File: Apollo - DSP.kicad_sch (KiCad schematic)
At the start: 27 parts, among them J1 USB_C_Receptacle_USB2.0, U1 NCP115ASN330T2G, U2 USBLC6-2SC6, U3 NCP115ASN330T2G

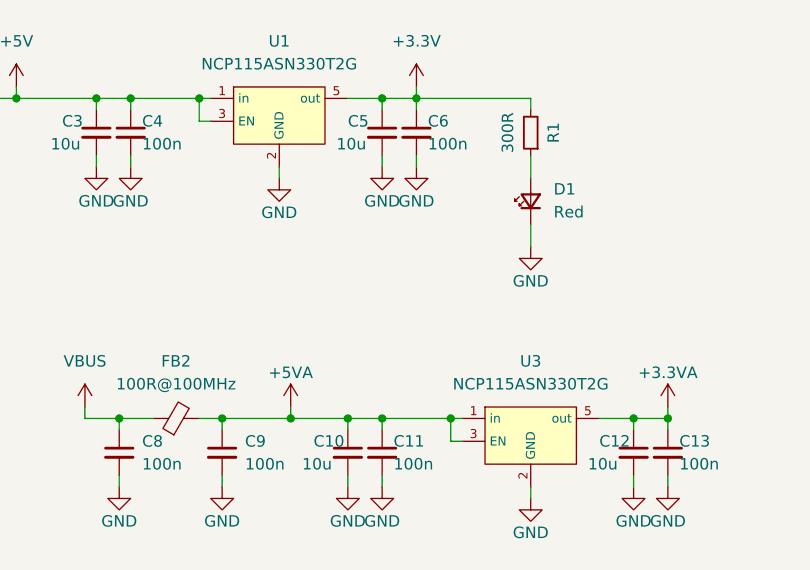
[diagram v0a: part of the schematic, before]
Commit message: made analog circuitry a bit more compact moved whole board
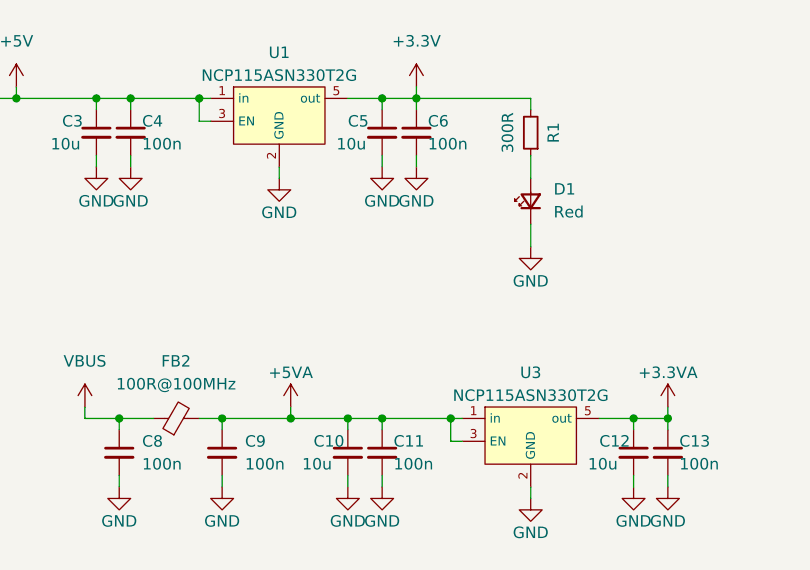
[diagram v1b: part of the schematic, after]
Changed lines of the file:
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@@
-    )
-  )
-  (symbol (lib_id "NCP115ASN330T2G:NCP115ASN330T2G") (at 160.02 71.12 0) (unit 1)
-    (in_bom yes) (on_board yes) (dnp no) (fields_autoplaced)
-    (property "Reference" "U1" (at 160.02 63.5 0)
-      (effects (font (size 1.27 1.27)))
-    )
-    (property "Value" "NCP115ASN330T2G" (at 160.02 66.04 0)
-      (effects (font (size 1.27 1.27)))
-    )
-    (property "Footprint" "NCP115ASN330T2G:NCP115ASN330T2G" (at 161.29 62.23 0)
-      (effects (font (size 1.27 1.27)) hide)
-    )
-    (property "Datasheet" "https://www.onsemi.com/pdf/datasheet/ncp115-d.pdf" (at 160.02 59.69 0)
-      (effects (font (size 1.27 1.27)) hide)
-    )
-    (pin "1")
-    (pin "2")
-    (pin "3")
-    (pin "5")
-    (instances
-      (project "Apollo - DSP"
-        (path "/e63e39d7-6ac0-4ffd-8aa3-1841a4541b55"
-          (reference "U1") (unit 1)
-        )
-      )
     )
   )
@@
         (path "/e63e39d7-6ac0-4ffd-8aa3-1841a4541b55"
           (reference "C10") (unit 1)
+        )
+      )
+    )
+  )
+  (symbol (lib_id "NCP115ASN330T2G:NCP115ASN330T2G") (at 160.02 71.12 0) (unit 1)
+    (in_bom yes) (on_board yes) (dnp no) (fields_autoplaced)
+    (property "Reference" "U1" (at 160.02 64.77 0)
+      (effects (font (size 1.27 1.27)))
+    )
+    (property "Value" "NCP115ASN330T2G" (at 160.02 67.31 0)
+      (effects (font (size 1.27 1.27)))
+    )
+    (property "Footprint" "NCP115ASN330T2G:NCP115ASN330T2G" (at 161.29 62.23 0)
+      (effects (font (size 1.27 1.27)) hide)
+    )
+    (property "Datasheet" "https://www.onsemi.com/pdf/datasheet/ncp115-d.pdf" (at 160.02 59.69 0)
+      (effects (font (size 1.27 1.27)) hide)
+    )
+    (pin "1")
+    (pin "2")
+    (pin "3")
+    (pin "5")
+    (instances
+      (project "Apollo - DSP"
+        (path "/e63e39d7-6ac0-4ffd-8aa3-1841a4541b55"
+          (reference "U1") (unit 1)
         )
       )
@@
     )
   )
-  (symbol (lib_id "power:VAA") (at 240.03 110.49 0) (unit 1)
-    (in_bom yes) (on_board yes) (dnp no)
-    (property "Reference" "#PWR0148" (at 240.03 114.3 0)
-      (effects (font (size 1.27 1.27)) hide)
-    )
-    (property "Value" "VAA" (at 240.03 106.68 0)
-      (effects (font (size 1.27 1.27)))
-    )
-    (property "Footprint" "" (at 240.03 110.49 0)
-      (effects (font (size 1.27 1.27)) hide)
-    )
-    (property "Datasheet" "" (at 240.03 110.49 0)
-      (effects (font (size 1.27 1.27)) hide)
-    )
-    (pin "1")
-    (instances
-      (project "Apollo - DSP"
-        (path "/e63e39d7-6ac0-4ffd-8aa3-1841a4541b55"
-          (reference "#PWR0148") (unit 1)
-        )
-      )
-    )
-  )
-  (symbol (lib_id "power:GND") (at 139.7 77.47 0) (unit 1)
-    (in_bom yes) (on_board yes) (dnp no)
-    (property "Reference" "#PWR0119" (at 139.7 83.82 0)
-      (effects (font (size 1.27 1.27)) hide)
-    )
-    (property "Value" "GND" (at 139.7 81.28 0)
-      (effects (font (size 1.27 1.27)))
-    )
-    (property "Footprint" "" (at 139.7 77.47 0)
-      (effects (font (size 1.27 1.27)) hide)
-    )
-    (property "Datasheet" "" (at 139.7 77.47 0)
-      (effects (font (size 1.27 1.27)) hide)
-    )
-    (pin "1")
-    (instances
-      (project "Apollo - DSP"
-        (path "/e63e39d7-6ac0-4ffd-8aa3-1841a4541b55"
-          (reference "#PWR0119") (unit 1)
-        )
-      )
-    )
-  )
-  (symbol (lib_id "power:+5VA") (at 161.29 104.14 0) (unit 1)
-    (in_bom yes) (on_board yes) (dnp no)
-    (property "Reference" "#PWR0132" (at 161.29 107.95 0)
-      (effects (font (size 1.27 1.27)) hide)
-    )
-    (property "Value" "+5VA" (at 161.29 100.33 0)
-      (effects (font (size 1.27 1.27)))
-    )
-    (property "Footprint" "" (at 161.29 104.14 0)
-      (effects (font (size 1.27 1.27)) hide)
-    )
-    (property "Datasheet" "" (at 161.29 104.14 0)
-      (effects (font (size 1.27 1.27)) hide)
-    )
-    (pin "1")
-    (instances
-      (project "Apollo - DSP"
-        (path "/e63e39d7-6ac0-4ffd-8aa3-1841a4541b55"
-          (reference "#PWR0132") (unit 1)
-        )
-      )
-    )
-  )
-  (symbol (lib_id "Device:C_Small") (at 203.2 109.22 0) (unit 1)
-    (in_bom yes) (on_board yes) (dnp no)
-    (property "Reference" "C13" (at 204.47 107.95 0)
-      (effects (font (size 1.27 1.27)) (justify left))
-    )
-    (property "Value" "100n" (at 204.47 110.49 0)
-      (effects (font (size 1.27 1.27)) (justify left))
-    )
-    (property "Footprint" "Capacitor_SMD:C_0603_1608Metric_Pad1.08x0.95mm_HandSolder" (at 203.2 109.22 0)
-      (effects (font (size 1.27 1.27)) hide)
-    )
-    (property "Datasheet" "~" (at 203.2 109.22 0)
-      (effects (font (size 1.27 1.27)) hide)
-    )
-    (pin "1")
-    (pin "2")
-    (instances
-      (project "Apollo - DSP"
-        (path "/e63e39d7-6ac0-4ffd-8aa3-1841a4541b55"
-          (reference "C13") (unit 1)
-        )
-      )
-    )
-  )
-  (symbol (lib_id "power:VBUS") (at 97.79 68.58 0) (unit 1)
-    (in_bom yes) (on_board yes) (dnp no) (fields_autoplaced)
-    (property "Reference" "#PWR0104" (at 97.79 72.39 0)
-      (effects (font (size 1.27 1.27)) hide)
-    )
-    (property "Value" "VBUS" (at 97.79 63.5 0)
-      (effects (font (size 1.27 1.27)))
-    )
-    (property "Footprint" "" (at 97.79 68.58 0)
-      (effects (font (size 1.27 1.27)) hide)
-    )
-    (property "Datasheet" "" (at 97.79 68.58 0)
-      (effects (font (size 1.27 1.27)) hide)
-    )
-    (pin "1")
-    (instances
-      (project "Apollo - DSP"
-        (path "/e63e39d7-6ac0-4ffd-8aa3-1841a4541b55"
-          (reference "#PWR0104") (unit 1)
-        )
-      )
-    )
-  )
   (symbol (lib_id "NCP115ASN330T2G:NCP115ASN330T2G") (at 187.96 106.68 0) (unit 1)
     (in_bom yes) (on_board yes) (dnp no) (fields_autoplaced)
-    (property "Reference" "U3" (at 187.96 99.06 0)
-      (effects (font (size 1.27 1.27)))
-    )
-    (property "Value" "NCP115ASN330T2G" (at 187.96 101.6 0)
+    (property "Reference" "U3" (at 187.96 100.33 0)
+      (effects (font (size 1.27 1.27)))
+    )
+    (property "Value" "NCP115ASN330T2G" (at 187.96 102.87 0)
       (effects (font (size 1.27 1.27)))
     )
@@
         )
       )
+    )
+  )
+  (symbol (lib_id "power:VAA") (at 240.03 110.49 0) (unit 1)
+    (in_bom yes) (on_board yes) (dnp no)
+    (property "Reference" "#PWR0148" (at 240.03 114.3 0)
+      (effects (font (size 1.27 1.27)) hide)
+    )
+    (property "Value" "VAA" (at 240.03 106.68 0)
+      (effects (font (size 1.27 1.27)))
+    )
+    (property "Footprint" "" (at 240.03 110.49 0)
+      (effects (font (size 1.27 1.27)) hide)
+    )
+    (property "Datasheet" "" (at 240.03 110.49 0)
+      (effects (font (size 1.27 1.27)) hide)
+    )
+    (pin "1")
+    (instances
+      (project "Apollo - DSP"
+        (path "/e63e39d7-6ac0-4ffd-8aa3-1841a4541b55"
+          (reference "#PWR0148") (unit 1)
+        )
+      )
+    )
+  )
+  (symbol (lib_id "power:GND") (at 139.7 77.47 0) (unit 1)
+    (in_bom yes) (on_board yes) (dnp no)
+    (property "Reference" "#PWR0119" (at 139.7 83.82 0)
+      (effects (font (size 1.27 1.27)) hide)
+    )
+    (property "Value" "GND" (at 139.7 81.28 0)
+      (effects (font (size 1.27 1.27)))
+    )
+    (property "Footprint" "" (at 139.7 77.47 0)
+      (effects (font (size 1.27 1.27)) hide)
+    )
+    (property "Datasheet" "" (at 139.7 77.47 0)
+      (effects (font (size 1.27 1.27)) hide)
+    )
+    (pin "1")
+    (instances
+      (project "Apollo - DSP"
+        (path "/e63e39d7-6ac0-4ffd-8aa3-1841a4541b55"
+          (reference "#PWR0119") (unit 1)
+        )
+      )
+    )
+  )
+  (symbol (lib_id "power:+5VA") (at 161.29 104.14 0) (unit 1)
+    (in_bom yes) (on_board yes) (dnp no)
+    (property "Reference" "#PWR0132" (at 161.29 107.95 0)
+      (effects (font (size 1.27 1.27)) hide)
+    )
+    (property "Value" "+5VA" (at 161.29 100.33 0)
+      (effects (font (size 1.27 1.27)))
+    )
+    (property "Footprint" "" (at 161.29 104.14 0)
+      (effects (font (size 1.27 1.27)) hide)
+    )
+    (property "Datasheet" "" (at 161.29 104.14 0)
+      (effects (font (size 1.27 1.27)) hide)
+    )
+    (pin "1")
+    (instances
+      (project "Apollo - DSP"
+        (path "/e63e39d7-6ac0-4ffd-8aa3-1841a4541b55"
+          (reference "#PWR0132") (unit 1)
+        )
+      )
+    )
+  )
+  (symbol (lib_id "Device:C_Small") (at 203.2 109.22 0) (unit 1)
+    (in_bom yes) (on_board yes) (dnp no)
+    (property "Reference" "C13" (at 204.47 107.95 0)
+      (effects (font (size 1.27 1.27)) (justify left))
+    )
+    (property "Value" "100n" (at 204.47 110.49 0)
+      (effects (font (size 1.27 1.27)) (justify left))
+    )
+    (property "Footprint" "Capacitor_SMD:C_0603_1608Metric_Pad1.08x0.95mm_HandSolder" (at 203.2 109.22 0)
+      (effects (font (size 1.27 1.27)) hide)
+    )
+    (property "Datasheet" "~" (at 203.2 109.22 0)
+      (effects (font (size 1.27 1.27)) hide)
+    )
+    (pin "1")
+    (pin "2")
+    (instances
+      (project "Apollo - DSP"
+        (path "/e63e39d7-6ac0-4ffd-8aa3-1841a4541b55"
+          (reference "C13") (unit 1)
+        )
+      )
+    )
+  )
+  (symbol (lib_id "power:VBUS") (at 97.79 68.58 0) (unit 1)
+    (in_bom yes) (on_board yes) (dnp no) (fields_autoplaced)
+    (property "Reference" "#PWR0104" (at 97.79 72.39 0)
+      (effects (font (size 1.27 1.27)) hide)
+    )
+    (property "Value" "VBUS" (at 97.79 63.5 0)
+      (effects (font (size 1.27 1.27)))
+    )
+    (property "Footprint" "" (at 97.79 68.58 0)
+      (effects (font (size 1.27 1.27)) hide)
+    )
+    (property "Datasheet" "" (at 97.79 68.58 0)
+      (effects (font (size 1.27 1.27)) hide)
+    )
+    (pin "1")
+    (instances
+      (project "Apollo - DSP"
+        (path "/e63e39d7-6ac0-4ffd-8aa3-1841a4541b55"
+          (reference "#PWR0104") (unit 1)
+        )
+      )

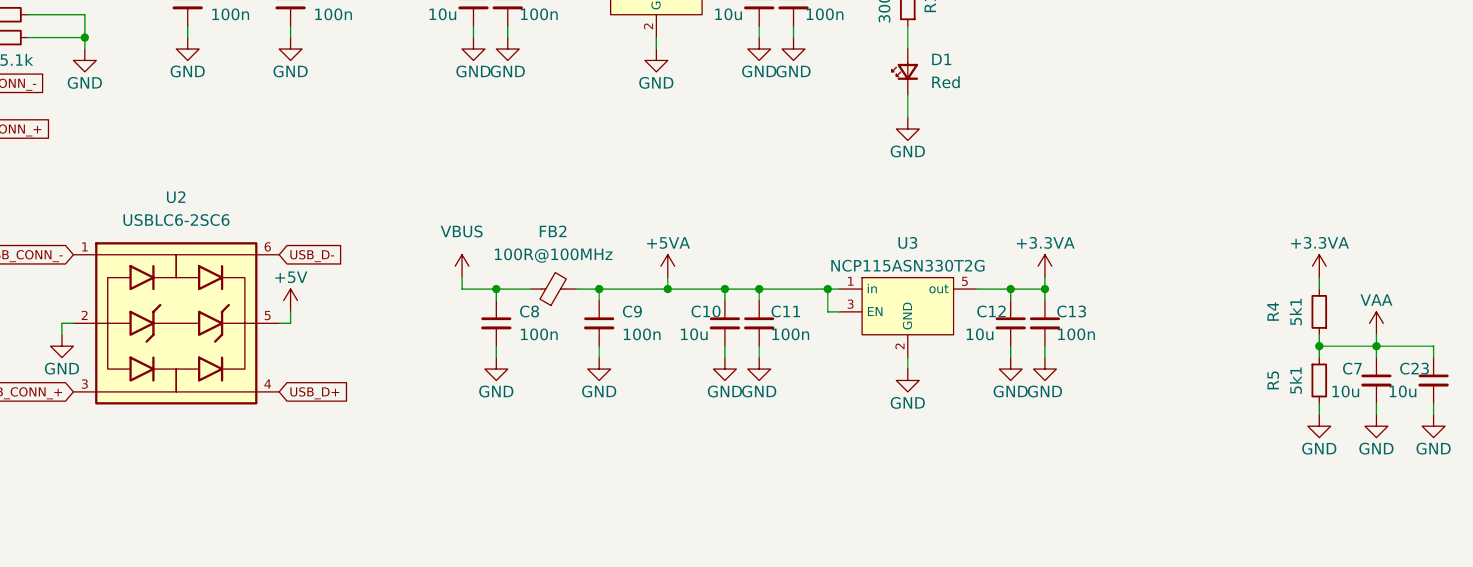
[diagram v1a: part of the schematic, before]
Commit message: added DAC and an onboard fixed oscilltor to quickly test the DSP
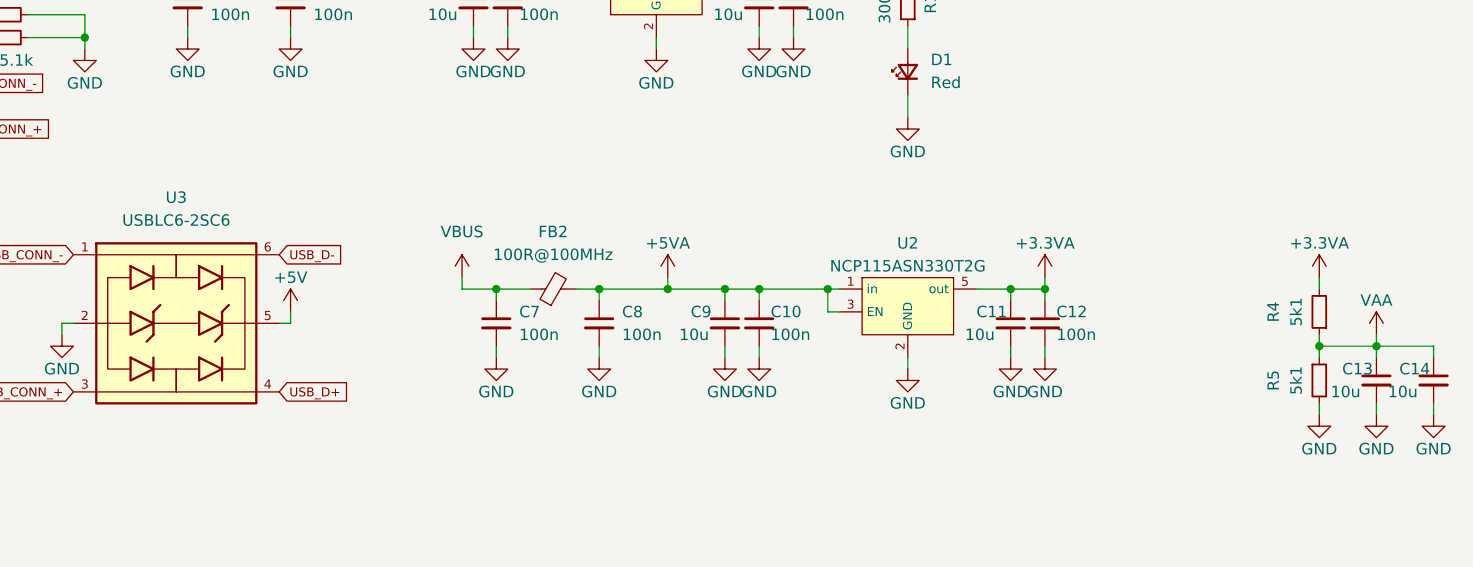
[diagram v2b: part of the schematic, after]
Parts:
- renumbered C11 to C10, C12 to C11, C13 to C12, C7 to C13, C23 to C14, C8 to C7, C9 to C8, C10 to C9, U3 to U2, U2 to U3

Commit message: cleanup
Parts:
- C1, C2, C7, C8: value 100n -> 10u
- F1: footprint Resistor_SMD:R_0603_1608Metric_Pad0.98x0.95mm_HandSolder -> Fuse:Fuse_0603_1608Metric_Pad1.05x0.95mm_HandSolder
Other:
- note added: "Xl = 2*pi*f*L L = Xl / 2*pi*f = 100R / (2*pi*100MHz) = 159nH fg = 1 / (2*pi*sqrt(L*C)) = 1 / (2*pi*sqrt(159nH*10uF)) = 126khz"
- moved on the sheet: C3
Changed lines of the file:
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@@
   (junction (at 80.01 82.55) (diameter 0) (color 0 0 0 0)
   )
+  (junction (at 138.43 69.85) (diameter 0) (color 0 0 0 0)
+  )
   (junction (at 203.2 105.41) (diameter 0) (color 0 0 0 0)
   )
@@
   (junction (at 171.45 69.85) (diameter 0) (color 0 0 0 0)
   )
-  (junction (at 130.81 69.85) (diameter 0) (color 0 0 0 0)
-  )
   (junction (at 161.29 105.41) (diameter 0) (color 0 0 0 0)
   )
@@
   (junction (at 96.52 77.47) (diameter 0) (color 0 0 0 0)
   )
+  (junction (at 129.54 69.85) (diameter 0) (color 0 0 0 0)
+  )
   (junction (at 107.95 69.85) (diameter 0) (color 0 0 0 0)
   )
@@
   )
   (junction (at 142.24 105.41) (diameter 0) (color 0 0 0 0)
-  )
-  (junction (at 139.7 69.85) (diameter 0) (color 0 0 0 0)
   )
   (junction (at 143.51 69.85) (diameter 0) (color 0 0 0 0)
@@
     (stroke (width 0) (type default))
   )
-  (wire (pts (xy 130.81 68.58) (xy 130.81 69.85))
+  (wire (pts (xy 129.54 68.58) (xy 129.54 69.85))
     (stroke (width 0) (type default))
   )
@@
     (stroke (width 0) (type default))
   )
-  (wire (pts (xy 139.7 69.85) (xy 143.51 69.85))
+  (wire (pts (xy 138.43 69.85) (xy 143.51 69.85))
     (stroke (width 0) (type default))
   )
@@
     (stroke (width 0) (type default))
   )
-  (wire (pts (xy 130.81 69.85) (xy 139.7 69.85))
+  (wire (pts (xy 129.54 69.85) (xy 138.43 69.85))
     (stroke (width 0) (type default))
   )
@@
     (stroke (width 0) (type default))
   )
-  (wire (pts (xy 139.7 76.2) (xy 139.7 77.47))
+  (wire (pts (xy 138.43 76.2) (xy 138.43 77.47))
     (stroke (width 0) (type default))
   )
@@
     (stroke (width 0) (type default))
   )
-  (wire (pts (xy 119.38 69.85) (xy 130.81 69.85))
+  (wire (pts (xy 119.38 69.85) (xy 129.54 69.85))
     (stroke (width 0) (type default))
   )
@@
     (stroke (width 0) (type default))
   )
-  (wire (pts (xy 139.7 71.12) (xy 139.7 69.85))
-    (stroke (width 0) (type default))
+  (wire (pts (xy 138.43 71.12) (xy 138.43 69.85))
+    (stroke (width 0) (type default))
+  )
+  (text "Xl = 2*pi*f*L\nL = Xl / 2*pi*f = 100R / (2*pi*100MHz) = 159nH\nfg = 1 / (2*pi*sqrt(L*C)) = 1 / (2*pi*sqrt(159nH*10uF)) = 126khz"
+    (at 139.7 128.27 0)
+    (effects (font (size 1.27 1.27)) (justify left bottom))
+  )
+  (text "Xl = 2*pi*f*L\nL = Xl / 2*pi*f = 100R / (2*pi*100MHz) = 159nH\nfg = 1 / (2*pi*sqrt(L*C)) = 1 / (2*pi*sqrt(159nH*10uF)) = 126khz"
+    (at 92.71 53.34 0)
+    (effects (font (size 1.27 1.27)) (justify left bottom))
   )
   (label "POW" (at 81.28 69.85 0) (fields_autoplaced)
@@
       (effects (font (size 1.27 1.27)) (justify left))
     )
-    (property "Value" "100n" (at 156.21 110.4962 0)
+    (property "Value" "10u" (at 156.21 110.4962 0)
       (effects (font (size 1.27 1.27)) (justify left))
     )
@@
     )
   )
-  (symbol (lib_id "power:+5V") (at 130.81 68.58 0) (unit 1)
+  (symbol (lib_id "power:+5V") (at 129.54 68.58 0) (unit 1)
     (in_bom yes) (on_board yes) (dnp no) (fields_autoplaced)
-    (property "Reference" "#PWR02" (at 130.81 72.39 0)
-      (effects (font (size 1.27 1.27)) hide)
-    )
-    (property "Value" "+5V" (at 130.81 63.5 0)
-      (effects (font (size 1.27 1.27)))
-    )
-    (property "Footprint" "" (at 130.81 68.58 0)
-      (effects (font (size 1.27 1.27)) hide)
-    )
-    (property "Datasheet" "" (at 130.81 68.58 0)
+    (property "Reference" "#PWR02" (at 129.54 72.39 0)
+      (effects (font (size 1.27 1.27)) hide)
+    )
+    (property "Value" "+5V" (at 129.54 63.5 0)
+      (effects (font (size 1.27 1.27)))
+    )
+    (property "Footprint" "" (at 129.54 68.58 0)
+      (effects (font (size 1.27 1.27)) hide)
+    )
+    (property "Datasheet" "" (at 129.54 68.58 0)
       (effects (font (size 1.27 1.27)) hide)
     )
@@
     )
   )
-  (symbol (lib_id "Device:C_Small") (at 139.7 73.66 0) (unit 1)
-    (in_bom yes) (on_board yes) (dnp no)
-    (property "Reference" "C3" (at 135.89 72.39 0)
-      (effects (font (size 1.27 1.27)) (justify left))
-    )
-    (property "Value" "10u" (at 134.62 74.93 0)
-      (effects (font (size 1.27 1.27)) (justify left))
-    )
-    (property "Footprint" "Capacitor_SMD:C_0603_1608Metric_Pad1.08x0.95mm_HandSolder" (at 139.7 73.66 0)
-      (effects (font (size 1.27 1.27)) hide)
-    )
-    (property "Datasheet" "~" (at 139.7 73.66 0)
+  (symbol (lib_id "Device:C_Small") (at 138.43 73.66 0) (unit 1)
+    (in_bom yes) (on_board yes) (dnp no)
+    (property "Reference" "C3" (at 134.62 72.39 0)
+      (effects (font (size 1.27 1.27)) (justify left))
+    )
+    (property "Value" "10u" (at 133.35 74.93 0)
+      (effects (font (size 1.27 1.27)) (justify left))
+    )
+    (property "Footprint" "Capacitor_SMD:C_0603_1608Metric_Pad1.08x0.95mm_HandSolder" (at 138.43 73.66 0)
+      (effects (font (size 1.27 1.27)) hide)
+    )
+    (property "Datasheet" "~" (at 138.43 73.66 0)
       (effects (font (size 1.27 1.27)) hide)
     )
@@
       (effects (font (size 1.27 1.27)) (justify left))
     )
-    (property "Value" "100n" (at 144.78 110.4962 0)
+    (property "Value" "10u" (at 144.78 110.4962 0)
       (effects (font (size 1.27 1.27)) (justify left))
     )
@@
     )
   )
-  (symbol (lib_id "power:GND") (at 139.7 77.47 0) (unit 1)
-    (in_bom yes) (on_board yes) (dnp no)
-    (property "Reference" "#PWR06" (at 139.7 83.82 0)
-      (effects (font (size 1.27 1.27)) hide)
-    )
-    (property "Value" "GND" (at 139.7 81.28 0)
-      (effects (font (size 1.27 1.27)))
-    )
-    (property "Footprint" "" (at 139.7 77.47 0)
-      (effects (font (size 1.27 1.27)) hide)
-    )
-    (property "Datasheet" "" (at 139.7 77.47 0)
+  (symbol (lib_id "power:GND") (at 138.43 77.47 0) (unit 1)
+    (in_bom yes) (on_board yes) (dnp no)
+    (property "Reference" "#PWR06" (at 138.43 83.82 0)
+      (effects (font (size 1.27 1.27)) hide)
+    )
+    (property "Value" "GND" (at 138.43 81.28 0)
+      (effects (font (size 1.27 1.27)))
+    )
+    (property "Footprint" "" (at 138.43 77.47 0)
+      (effects (font (size 1.27 1.27)) hide)
+    )
+    (property "Datasheet" "" (at 138.43 77.47 0)
       (effects (font (size 1.27 1.27)) hide)
     )
@@
       (effects (font (size 1.27 1.27)) (justify left))
     )
-    (property "Value" "100n" (at 121.92 74.9362 0)
+    (property "Value" "10u" (at 121.92 74.9362 0)
       (effects (font (size 1.27 1.27)) (justify left))
     )
@@
       (effects (font (size 1.27 1.27)) (justify left))
     )
-    (property "Value" "100n" (at 110.49 74.9362 0)
+    (property "Value" "10u" (at 110.49 74.9362 0)
       (effects (font (size 1.27 1.27)) (justify left))
     )
@@
       (effects (font (size 1.27 1.27)))
     )
-    (property "Footprint" "Resistor_SMD:R_0603_1608Metric_Pad0.98x0.95mm_HandSolder" (at 90.17 71.628 90)
-      (effects (font (size 1.27 1.27)) hide)
-    )
+    (property "Footprint" "Fuse:Fuse_0603_1608Metric_Pad1.05x0.95mm_HandSolder" (at 90.17 71.628 90)
+      (effects (font (size 1.27 1.27)) hide)
+    )
